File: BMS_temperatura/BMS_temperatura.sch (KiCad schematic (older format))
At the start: 75 parts, among them J101 Conn_01x08_Male, Q101 MMBT3904, U1 UFRGS_PILL, U101 74HC4051, U103 74HC4051, U105 74HC4051, U110 MCP2558, U112 LM324

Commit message: layout att 3
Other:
- moved on the sheet: C116, C117, R110, R111, R112, U110

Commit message: layout bms temp pronto
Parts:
- G101: footprint e-Power:Logo_UFRGS_22.0x12.0mm_Mask -> e-Power:Logo_UFRGS_9.2x5.0mm_SilkS
- G102: footprint e-Power:Logo_e-Power_22.8x12.0mm_SilkS -> e-Power:Logo_e-Power_12.4x6.0mm_SilkS
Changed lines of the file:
@@
 F 0 "G101" H 5000 9400 60  0000 C CNN
 F 1 "Logo_UFRGS_Large" H 5000 9800 60  0001 C CNN
-F 2 "e-Power:Logo_UFRGS_22.0x12.0mm_Mask" H 5000 9300 50  0000 C CNN
+F 2 "e-Power:Logo_UFRGS_9.2x5.0mm_SilkS" H 5000 9300 50  0000 C CNN
 F 3 "" H 5000 9600 50  0001 C CNN
 	1    5000 9600
@@
 F 0 "G102" H 5000 8975 60  0000 C CNN
 F 1 "Logo_e-Power_Large" H 5000 9350 60  0001 C CNN
-F 2 "e-Power:Logo_e-Power_22.8x12.0mm_SilkS" H 5000 8900 50  0000 C CNN
+F 2 "e-Power:Logo_e-Power_12.4x6.0mm_SilkS" H 5000 8900 50  0000 C CNN
 F 3 "" H 5000 9150 50  0001 C CNN
 	1    5000 9150
@@
 	1    0    0    -1
 $EndComp
-Wire Bus Line
-	1200 4100 1200 4800
-Wire Bus Line
-	1200 2650 1200 3350
-Wire Bus Line
-	2850 6250 2850 6950
-Wire Bus Line
-	1200 6250 1200 6950
-Wire Bus Line
-	1200 5450 1200 6150
-Wire Bus Line
-	1200 1200 1200 1900
 Wire Wire Line
 	5000 1100 5150 1100
 Text Label 5150 1100 0    50   ~ 0
 5.000V
+Wire Bus Line
+	1200 4100 1200 4800
+Wire Bus Line
+	1200 2650 1200 3350
+Wire Bus Line
+	2850 6250 2850 6950
+Wire Bus Line
+	1200 6250 1200 6950
+Wire Bus Line
+	1200 5450 1200 6150
+Wire Bus Line
+	1200 1200 1200 1900
 $EndSCHEMATC

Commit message: layout final bms temp
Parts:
- removed TP12: C_ERROR, e-Power:TestPoint_Pad_D1.0mm, symbol Connector:TestPoint
- removed TP13: T_ERROR, e-Power:TestPoint_Pad_D1.0mm, symbol Connector:TestPoint
- removed TP14: TOUT_3P, e-Power:TestPoint_Pad_D1.0mm, symbol Connector:TestPoint
- TP10: value TOUT_3P -> TOUT_1P
- TP11: value VCC -> ~ERROR
- TP2: value TOUT_3P -> TOUT_2P
- TP22: value VCC -> GNG
- TP6: value TX -> RX
- TP7: value RX -> TX
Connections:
- net +12V: now reaches U1.40 (VIN)
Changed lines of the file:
@@
 P 5150 4950
 F 0 "TP2" V 5150 5138 50  0000 L CNN
-F 1 "TOUT_3P" V 5195 5138 50  0001 L CNN
+F 1 "TOUT_2P" V 5195 5138 50  0001 L CNN
 F 2 "e-Power:TestPoint_Pad_D1.0mm" H 5350 4950 50  0001 C CNN
 F 3 "~" H 5350 4950 50  0001 C CNN
 	1    5150 4950
 	0    -1   -1   0
-$EndComp
-$Comp
-L Connector:TestPoint TP14
-U 1 1 61149042
-P 7000 5450
-F 0 "TP14" V 7000 5638 50  0000 L CNN
-F 1 "TOUT_3P" V 7045 5638 50  0001 L CNN
-F 2 "e-Power:TestPoint_Pad_D1.0mm" H 7200 5450 50  0001 C CNN
-F 3 "~" H 7200 5450 50  0001 C CNN
-	1    7000 5450
-	0    1    1    0
 $EndComp
 $Comp
@@
 P 6850 5650
 F 0 "TP10" V 6850 5838 50  0000 L CNN
-F 1 "TOUT_3P" V 6895 5838 50  0001 L CNN
+F 1 "TOUT_1P" V 6895 5838 50  0001 L CNN
 F 2 "e-Power:TestPoint_Pad_D1.0mm" H 7050 5650 50  0001 C CNN
 F 3 "~" H 7050 5650 50  0001 C CNN
@@
 P 5400 5450
 F 0 "TP6" V 5400 5638 50  0000 L CNN
-F 1 "TX" V 5445 5638 50  0001 L CNN
+F 1 "RX" V 5445 5638 50  0001 L CNN
 F 2 "e-Power:TestPoint_Pad_D1.0mm" H 5600 5450 50  0001 C CNN
 F 3 "~" H 5600 5450 50  0001 C CNN
@@
 P 5400 5550
 F 0 "TP7" V 5400 5738 50  0000 L CNN
-F 1 "RX" V 5445 5738 50  0001 L CNN
+F 1 "TX" V 5445 5738 50  0001 L CNN
 F 2 "e-Power:TestPoint_Pad_D1.0mm" H 5600 5550 50  0001 C CNN
 F 3 "~" H 5600 5550 50  0001 C CNN
@@
 Text Label 6600 5250 0    50   ~ 0
 T_ERROR
-$Comp
-L Connector:TestPoint TP13
-U 1 1 612E123F
-P 7000 5250
-F 0 "TP13" V 7000 5438 50  0000 L CNN
-F 1 "T_ERROR" V 7045 5438 50  0001 L CNN
-F 2 "e-Power:TestPoint_Pad_D1.0mm" H 7200 5250 50  0001 C CNN
-F 3 "~" H 7200 5250 50  0001 C CNN
-	1    7000 5250
-	0    1    1    0
-$EndComp
 Wire Wire Line
 	6550 5250 7000 5250
 Wire Wire Line
 	6550 5150 7000 5150
-$Comp
-L Connector:TestPoint TP12
-U 1 1 61300E5F
-P 7000 5150
-F 0 "TP12" V 7000 5338 50  0000 L CNN
-F 1 "C_ERROR" V 7045 5338 50  0001 L CNN
-F 2 "e-Power:TestPoint_Pad_D1.0mm" H 7200 5150 50  0001 C CNN
-F 3 "~" H 7200 5150 50  0001 C CNN
-	1    7000 5150
-	0    1    1    0
-$EndComp
 Text Label 6600 5150 0    50   ~ 0
 COMM_ERROR
@@
 P 7000 1650
 F 0 "TP11" V 7000 1838 50  0000 L CNN
-F 1 "VCC" V 7045 1838 50  0001 L CNN
+F 1 "~ERROR" V 7045 1838 50  0001 L CNN
 F 2 "e-Power:TestPoint_Pad_D1.0mm" H 7200 1650 50  0001 C CNN
 F 3 "~" H 7200 1650 50  0001 C CNN
@@
 P 7650 1850
 F 0 "TP22" V 7650 2038 50  0000 L CNN
-F 1 "VCC" V 7695 2038 50  0001 L CNN
+F 1 "GNG" V 7695 2038 50  0001 L CNN
 F 2 "e-Power:TestPoint_Pad_D1.0mm" H 7850 1850 50  0001 C CNN
 F 3 "~" H 7850 1850 50  0001 C CNN
@@
 Text Label 5150 1100 0    50   ~ 0
 5.000V
+$Comp
+L power:+12V #PWR?
+U 1 1 606CA144
+P 6550 4250
+AR Path="/5ED9340F/606CA144" Ref="#PWR?"  Part="1"
+AR Path="/606CA144" Ref="#PWR0104"  Part="1"
+F 0 "#PWR0104" H 6550 4100 50  0001 C CNN
+F 1 "+12V" H 6565 4423 50  0000 C CNN
+F 2 "" H 6550 4250 50  0001 C CNN
+F 3 "" H 6550 4250 50  0001 C CNN
+	1    6550 4250
+	1    0    0    -1
+$EndComp
+Wire Wire Line
+	6550 4350 6550 4250
 Wire Bus Line
 	1200 4100 1200 4800

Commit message: Add files via upload
Divisor de tensão
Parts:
- added R1, R4, R5: 10k, Resistor_SMD:R_0805_2012Metric, symbol BMS_temperatura-rescue:R-Device
- added R2, R3: 1k, Resistor_SMD:R_0805_2012Metric, symbol BMS_temperatura-rescue:R-Device
- C101, C103, C106, C116, C117, C125: symbol Device:C -> BMS_temperatura-rescue:C-Device
- D101, D102, D104: symbol Device:LED -> BMS_temperatura-rescue:LED-Device
- G101: symbol e-Power:Logo_UFRGS_Large -> BMS_temperatura-rescue:Logo_UFRGS_Large-e-Power
- G102: symbol e-Power:Logo_e-Power_Large -> BMS_temperatura-rescue:Logo_e-Power_Large-e-Power
- G104: symbol Graphic:SYM_LASER_Large -> BMS_temperatura-rescue:SYM_LASER_Large-Graphic
- H101, H102, H103, H104: symbol Mechanical:MountingHole_Pad -> BMS_temperatura-rescue:MountingHole_Pad-Mechanical
- J101: symbol Connector:Conn_01x08_Male -> BMS_temperatura-rescue:Conn_01x08_Male-Connector
- Q101: symbol Transistor_BJT:MMBT3904 -> BMS_temperatura-rescue:MMBT3904-Transistor_BJT
- R101, R103, R104, R105, R107, R110, R111, R112, R113, R114, R115, R116, R117, R118, R123, R124, R125, R126, R127, R129, R134, R135, R136, R141, R142, R143, R144, R145, R146: symbol Device:R -> BMS_temperatura-rescue:R-Device
- TP1, TP10, TP11, TP15, TP16, TP17, TP18, TP19, TP2, TP20, TP21, TP22, TP3, TP4, TP5, TP6, TP7, TP8, TP9: symbol Connector:TestPoint -> BMS_temperatura-rescue:TestPoint-Connector
- U1: symbol e-Power:UFRGS_PILL -> BMS_temperatura-rescue:UFRGS_PILL-e-Power
- U101, U103, U105: symbol 74xx:74HC4051 -> BMS_temperatura-rescue:74HC4051-74xx
- U110: symbol Interface_CAN_LIN:MCP2558FD-xSN -> BMS_temperatura-rescue:MCP2558FD-xSN-Interface_CAN_LIN
- U112: symbol Amplifier_Operational:LM324 -> BMS_temperatura-rescue:LM324-Amplifier_Operational
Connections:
- net GND: now also R4.2, R5.2
- new net: R2.1, R3.2
- new net: R1.1, R2.2
- new net Output: R3.1, R4.1, R5.1
- new net Signal_bateria_baixa: R1.2
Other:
- note added: "16,8 V - 4,94 V"

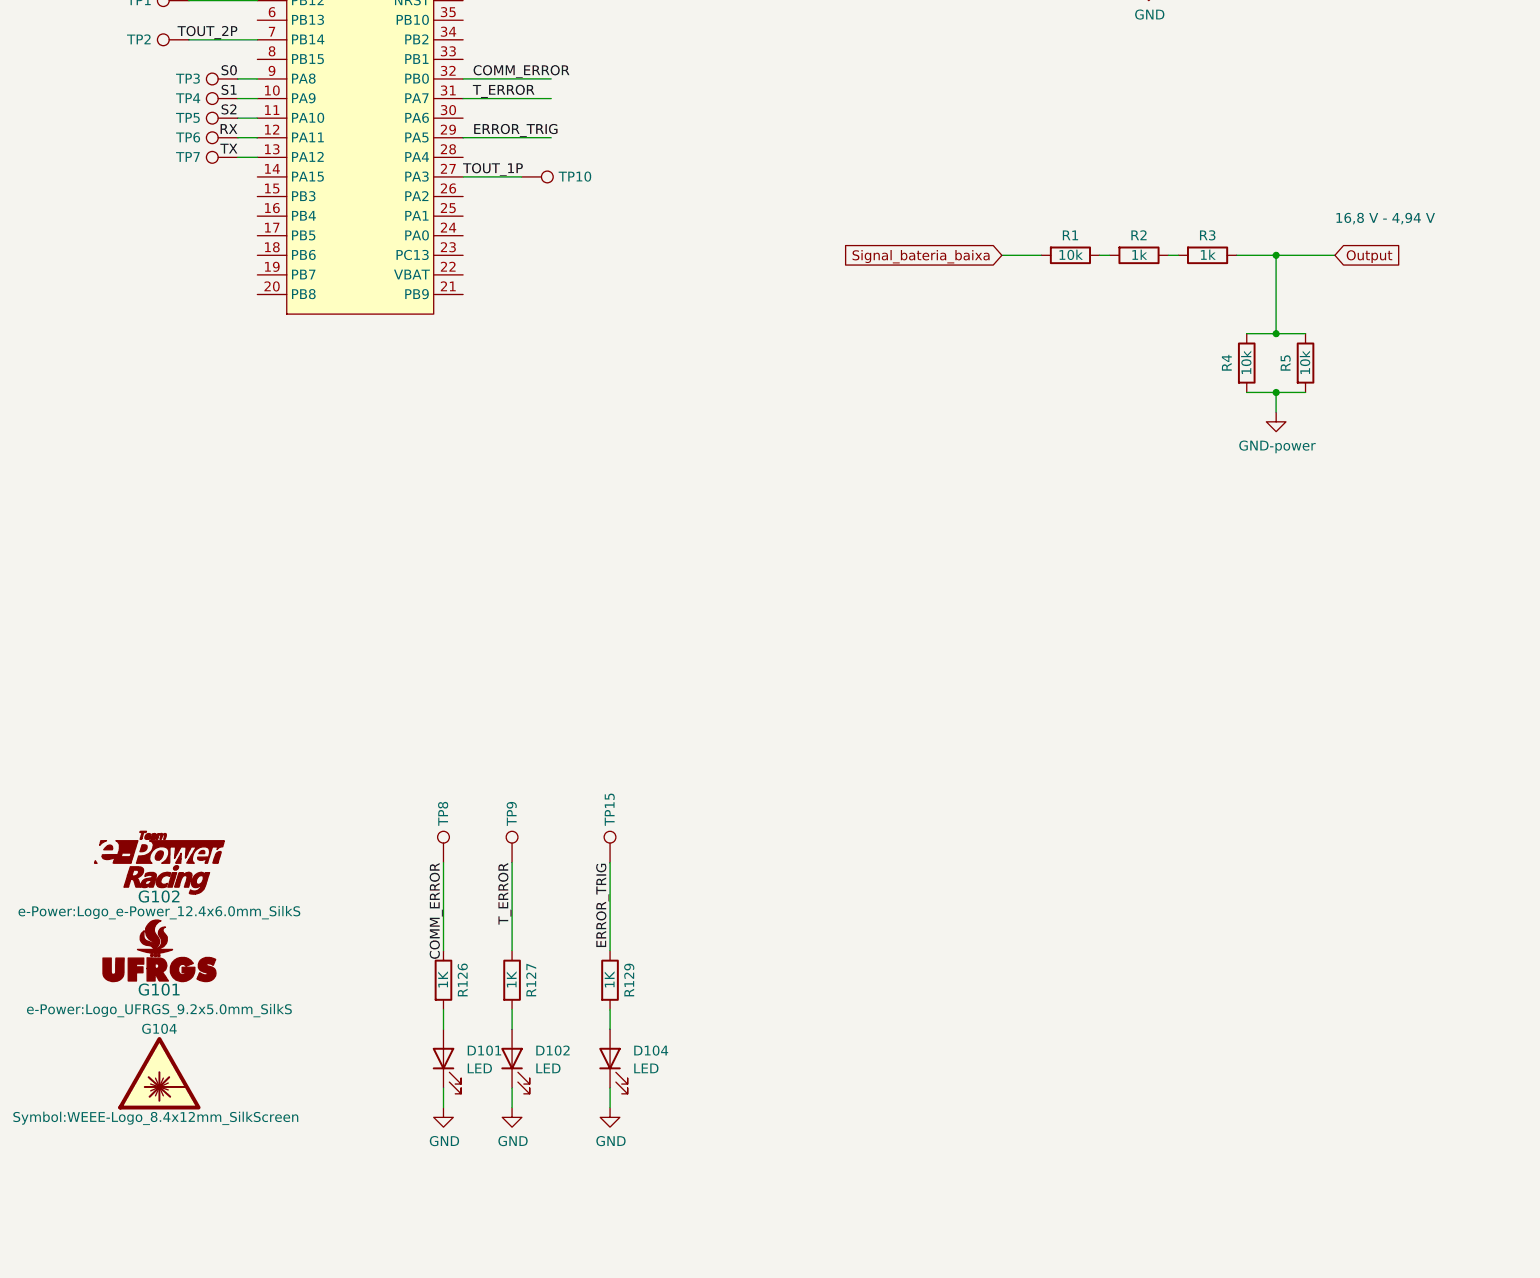
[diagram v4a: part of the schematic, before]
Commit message: Placa BMS-temperatura
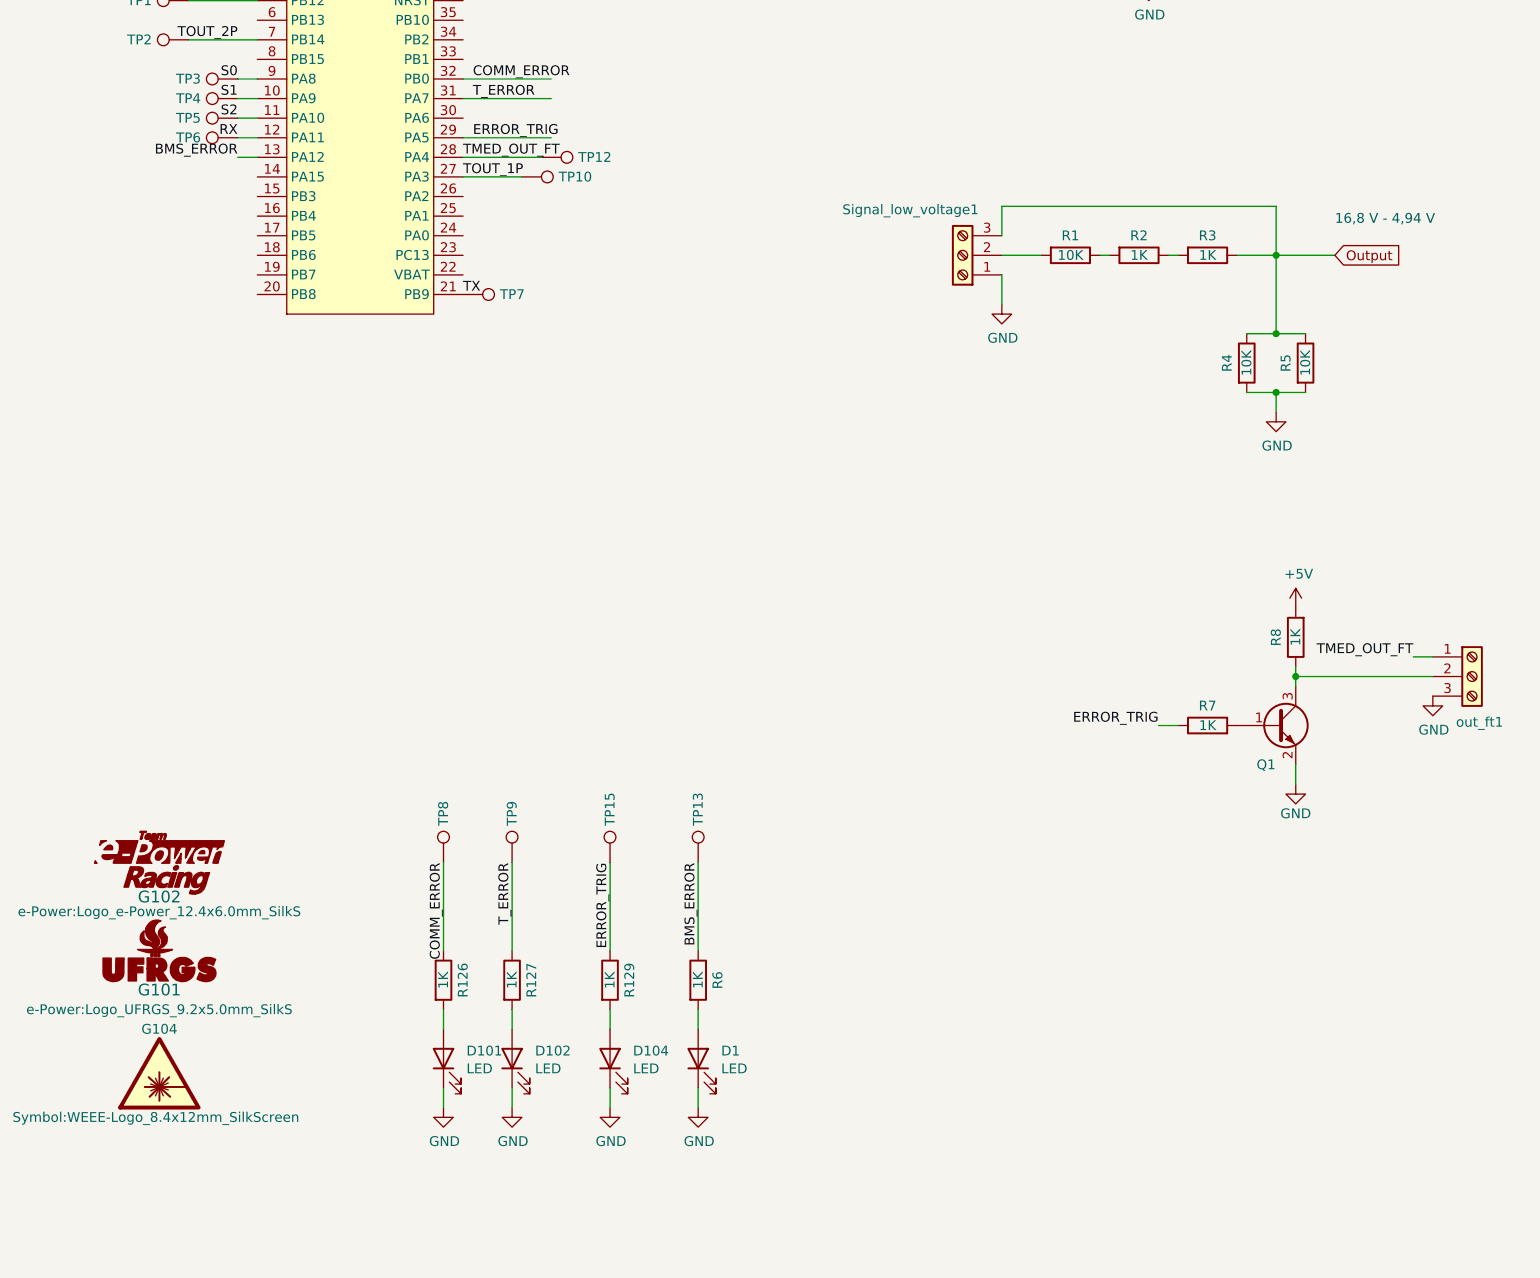
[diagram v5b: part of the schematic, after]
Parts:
- added D1: LED, e-Power:LED_0805_1.15x1.40mm_HandSolder, symbol BMS_temperatura-rescue:LED-Device
- added Q1: MMBT3904, Package_TO_SOT_SMD:SOT-23, symbol BMS_temperatura-rescue:MMBT3904-Transistor_BJT
- added R6, R7, R8: 1K, Resistor_SMD:R_0805_2012Metric, symbol BMS_temperatura-rescue:R-Device
- added Signal_low_voltage1, out_ft1: Screw_Terminal_01x03, e-Power:TerminalBlock_Phoenix_MKDS-1,5-3_1x03_P5.00mm_Horizontal, symbol Connector:Screw_Terminal_01x03
- added TP12: TMED_OUT_FT, e-Power:TestPoint_Pad_D1.0mm, symbol BMS_temperatura-rescue:TestPoint-Connector
- added TP13: BMS_ERROR, e-Power:TestPoint_Pad_D1.0mm, symbol BMS_temperatura-rescue:TestPoint-Connector
- R1, R4, R5: value 10k -> 10K; LCSC C17415 -> C17513
- R2, R3: value 1k -> 1K; LCSC C17415 -> C17513
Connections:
- net +5V: now also R8.2
- net ERROR_TRIG: now also R7.1
- net GND: now also D1.1 (K), Q1.2 (E), Signal_low_voltage1.1 (Pin_1), out_ft1.3 (Pin_3)
- net Output: now also Signal_low_voltage1.3 (Pin_3)
- net TX: now also U1.21 (PB9); no longer U1.13 (PA12)
- net TMED_OUT_FT: now reaches U1.28 (PA4)
- net TMED_OUT_FT: now also TP12.1, out_ft1.1 (Pin_1)
- net Signal_bateria_baixa: no longer names the net of R1.2
- net Signal_bateria_baixa: now also Signal_low_voltage1.2 (Pin_2)
- new net: Q1.3 (C), R8.1, out_ft1.2 (Pin_2)
- new net: D1.2 (A), R6.2
- new net: Q1.1 (B), R7.2
- new net BMS_ERROR: R6.1, TP13.1, U1.13 (PA12)
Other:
- moved on the sheet: TP7
